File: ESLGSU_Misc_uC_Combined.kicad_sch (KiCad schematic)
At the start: 5 parts, among them U57 CY8C9520A, U74 PCAL6524HEAZ

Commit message: Finished initial revision of PCB
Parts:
- added U93: ~, ESLGSU_Parts_Lib:PROTO, symbol ESLGSU_Parts_Lib:PROTO
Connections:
- net GND: now also U93.4 (GND)
- net GPIO_1: now also U93.5 (GPIO1)
- net GPIO_2: now also U93.6 (GPIO2)
- net GPIO_3: now also U93.7 (GPIO3)
- net GPIO_4: now also U93.8 (GPIO4)
- net GPIO_5: now also U93.9 (GPIO5)
- net GPIO_6: now also U93.10 (GPIO6)
- net GPIO_7: now also U93.11 (GPIO7)
- net GPIO_8: now also U93.12 (GPIO8)
- net I2C1_SCL: now also U93.17 (SCL)
- net I2C1_SDA: now also U93.18 (SDA)
- net PISER_RX: now also U93.19 (RX)
- net PISER_TX: now also U93.20 (TX)
- net PISPI_MISO: now also U93.13 (MISO)
- net PISPI_MOSI: now also U93.14 (MOSI)
- net PISPI_SCK: now also U93.15 (SCK)
- net PI_SS_MISC2: now also U93.16 (NSS)
- new net M1SUB3V3: U93.2 (SUB3V3)
- new net M1SUB5V: U93.1 (SUB5V)
- new net M1VBUS: U93.3 (VTRX)
- no-connect marks 14 -> 17
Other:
- sheet Misc_uCs ports: added SUB3V3, SUB5V, VBUS; removed none
- sheet Misc_uCs1 ports: added SUB3V3, SUB5V, VBUS; removed none

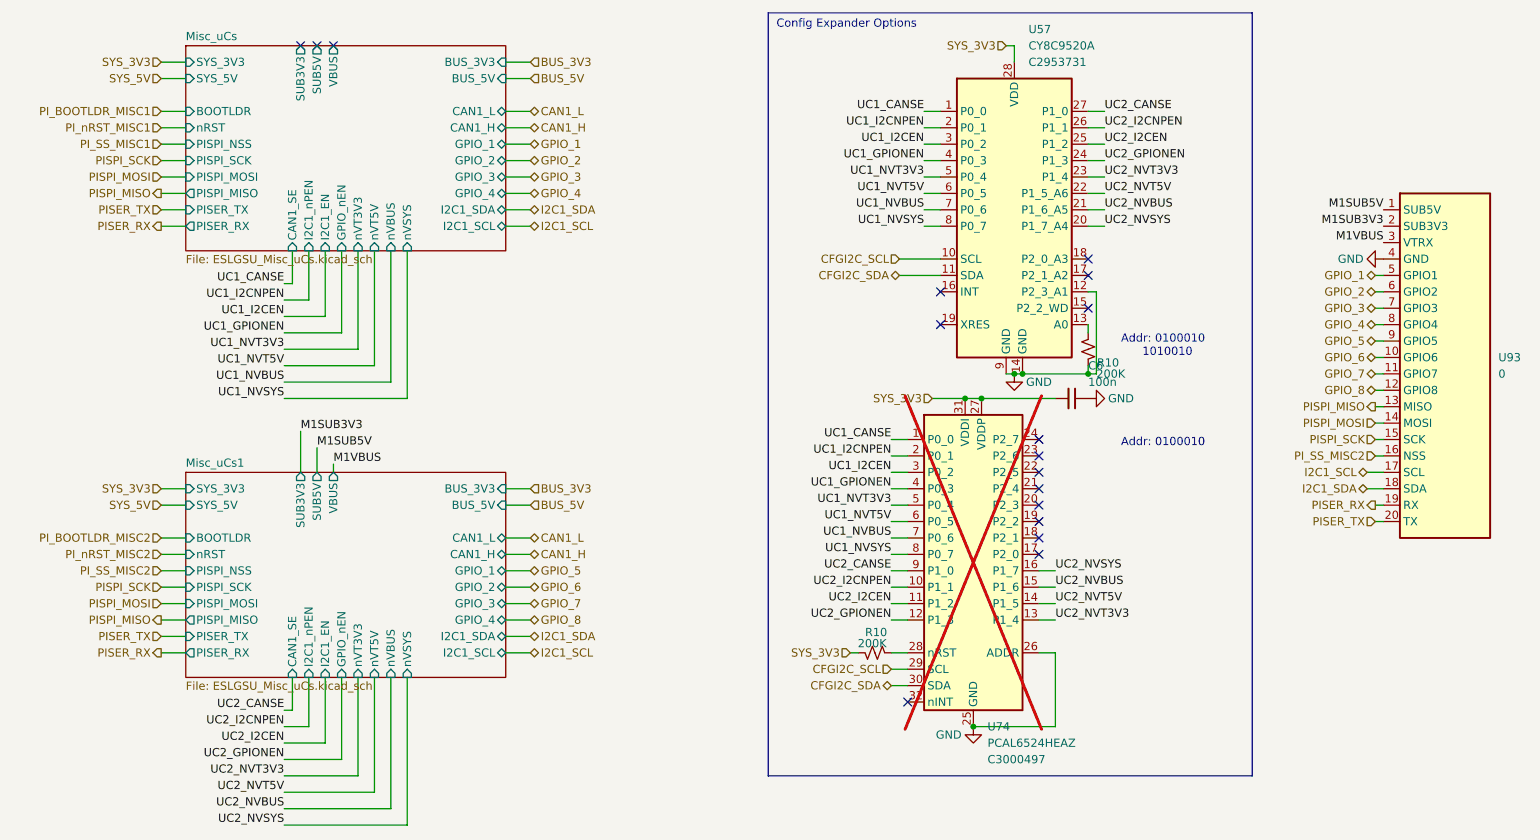
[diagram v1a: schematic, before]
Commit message: Removed some parts
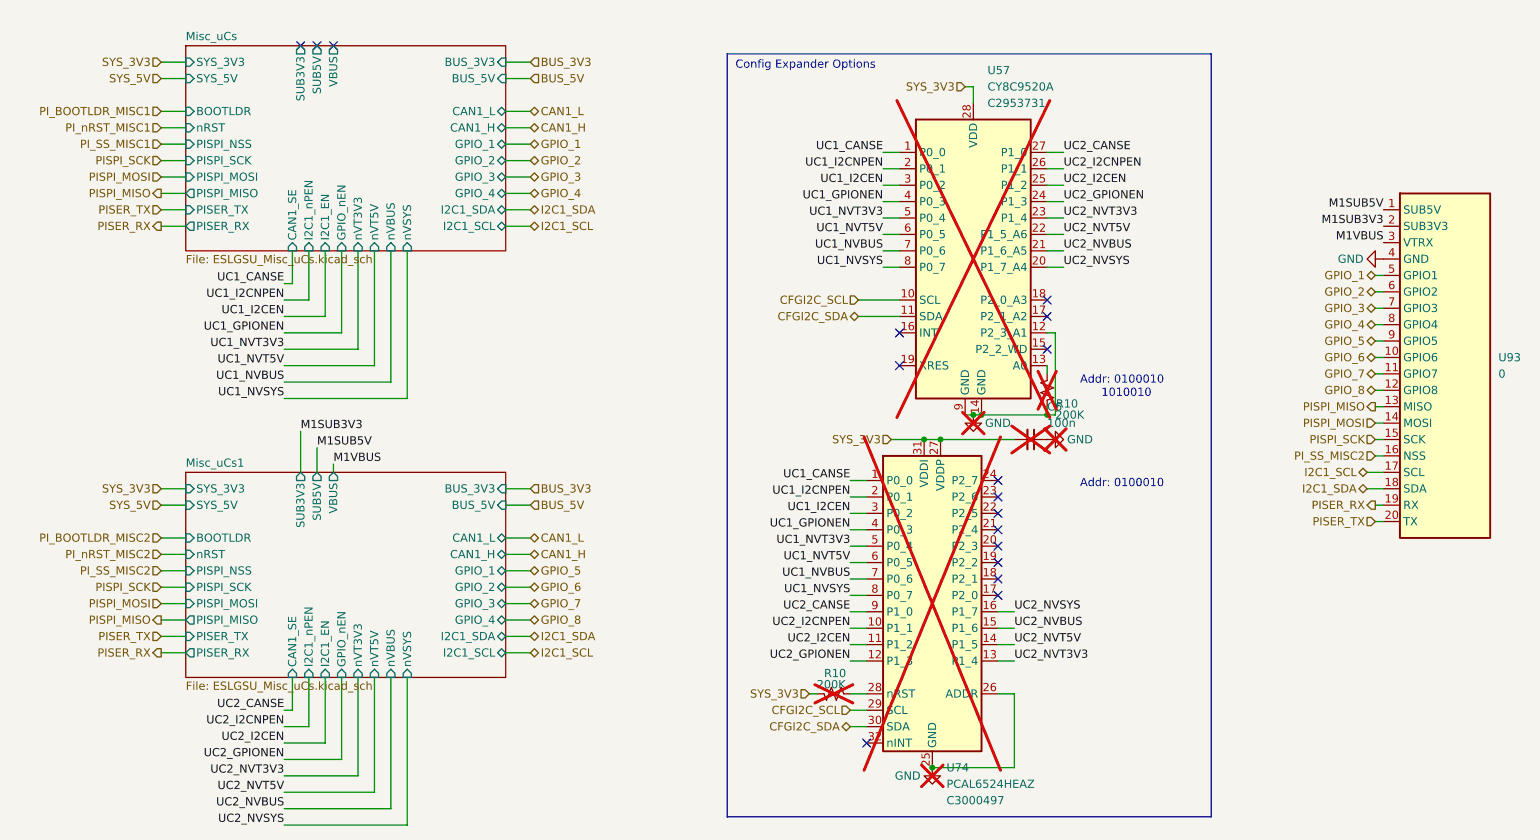
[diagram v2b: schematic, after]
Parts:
- removed R10 (x2): 200K, Resistor_SMD:R_0402_1005Metric, symbol Device:R_Small_US
- added R10 (x2): 200K, Resistor_SMD:R_0402_1005Metric, symbol Device:R_Small_US
- C6, U57: now not fitted; now left out of the parts list
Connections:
- net GND: now also R10.1
- net SYS_3V3: now also R10.1
- net at U74.28 (nRST): now also R10.2
- net at U57.13 (A0): now also R10.2
